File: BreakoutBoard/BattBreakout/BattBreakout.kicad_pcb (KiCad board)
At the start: 2 copper layers, 67.3 x 52.1 mm, 24 parts, among them Q4 IPB180N10S4-02, Q9 IPB180N10S4-02, U2 LM5050MK-1_NOPB, U3 LM5050MK-1_NOPB

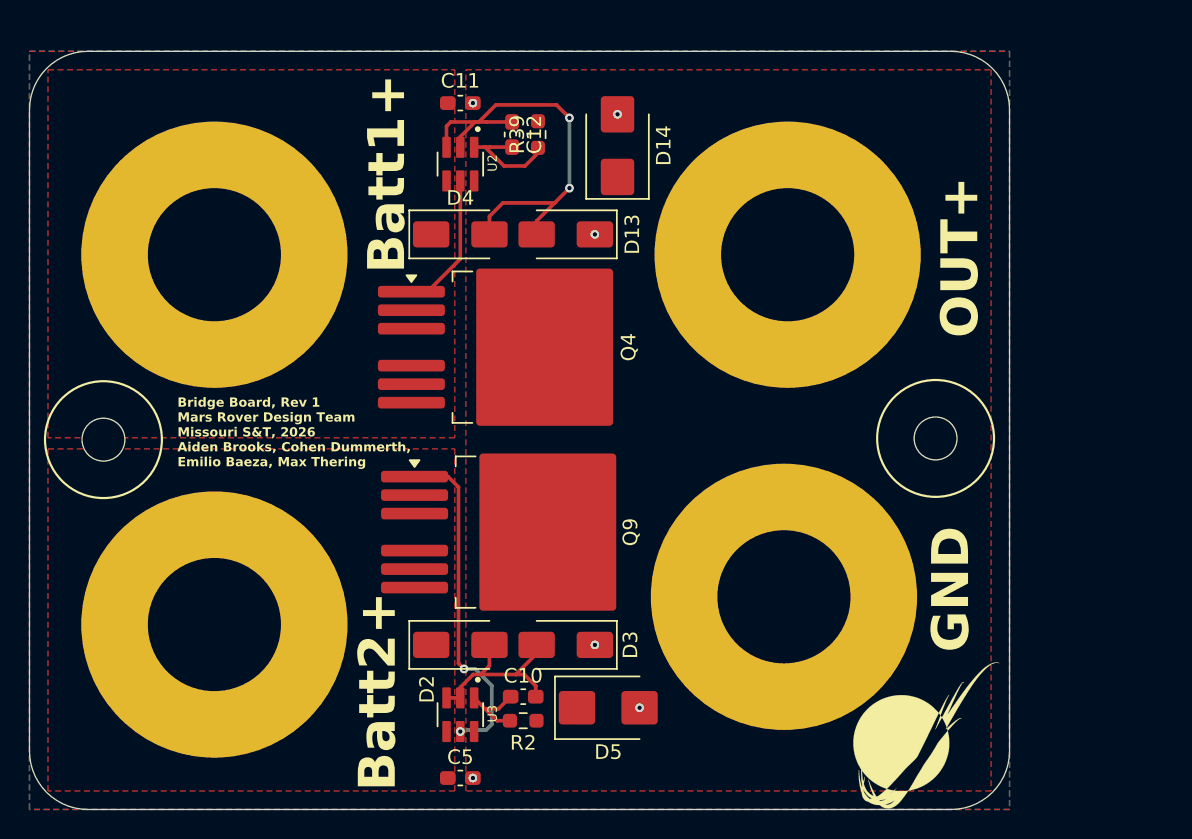
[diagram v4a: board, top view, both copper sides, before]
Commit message: Updated mosfet in schematic
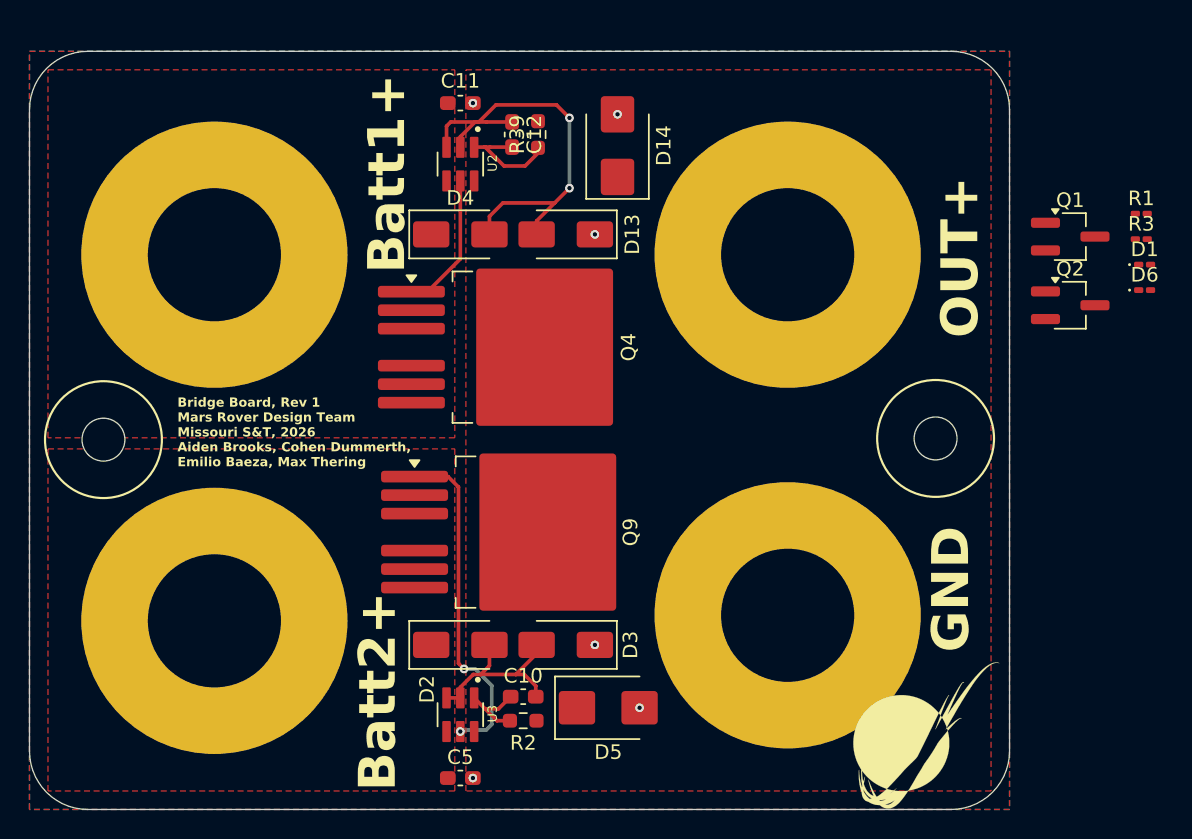
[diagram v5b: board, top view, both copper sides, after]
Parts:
- added D1: GRN, LED_SMD:LED_0201_0603Metric_Pad0.64x0.40mm_HandSolder, F.Cu at (107.1, 52.8)
- added D6: GRN, LED_SMD:LED_0201_0603Metric_Pad0.64x0.40mm_HandSolder, F.Cu at (107.1, 54.5)
- added Q1: BSS138, Package_TO_SOT_SMD:SOT-23W_Handsoldering, F.Cu at (102.0, 50.8)
- added Q2: BSS138, Package_TO_SOT_SMD:SOT-23W_Handsoldering, F.Cu at (102.0, 55.5)
- added R1: 6.8k, Resistor_SMD:R_0201_0603Metric_Pad0.64x0.40mm_HandSolder, F.Cu at (106.8, 49.2)
- added R3: 6.8k, Resistor_SMD:R_0201_0603Metric_Pad0.64x0.40mm_HandSolder, F.Cu at (106.8, 51.0)
- moved V3 39.4 mm to (82.5, 76.8)
- moved V2 39.2 mm to (43.2, 77.2)

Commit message: Added LEDS to layout
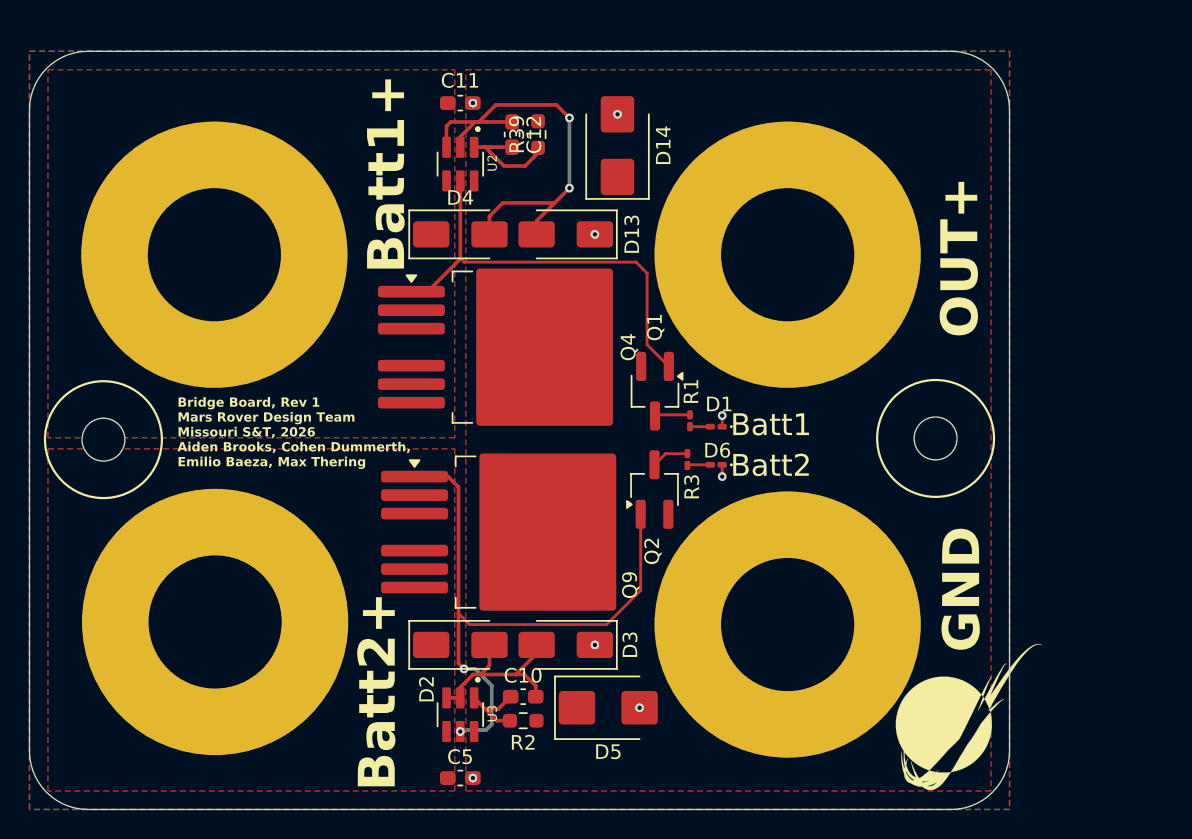
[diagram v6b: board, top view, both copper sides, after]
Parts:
- moved V2 39.4 mm to (82.5, 77.5)
- moved V3 39.3 mm to (43.2, 77.3)
- moved R3 34.7 mm to (75.7, 66.1), turned to 90 degrees
- moved R1 34.1 mm to (75.8, 63.5), turned to 90 degrees
- moved D6 31.8 mm to (77.6, 66.5), turned to 180 degrees
- moved D1 31.5 mm to (77.6, 63.9), turned to 180 degrees
- moved Q2 31.2 mm to (73.4, 68.2), turned to 90 degrees
- moved Q1 30.4 mm to (73.4, 61.4), turned to -90 degrees
- moved G1 3.19 mm to (95.0, 83.8)
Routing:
- net Net-(Q1-G): track 9.65 -> 29.9 mm
- net Net-(Q2-G): track 23.4 -> 42.4 mm
- net Net-(Q2-D): track 0.00 -> 2.58 mm
- net Net-(Q1-D): track 0.00 -> 2.44 mm
- net Net-(D6-A): track 0.00 -> 1.59 mm
- net GND: track 0.00 -> 1.58 mm, vias 6 -> 8
- net Net-(D1-A): track 0.00 -> 1.40 mm
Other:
- board text added: "Batt1"
- board text added: "Batt2"

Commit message: Fixed resistor footprints
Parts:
- R2, R39: footprint Resistor_SMD:R_0603_1608Metric_Pad0.98x0.95mm_HandSolder -> Resistor_SMD:R_0201_0603Metric_Pad0.64x0.40mm_HandSolder
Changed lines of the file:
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@@
 		)
 	)
-	(footprint "Resistor_SMD:R_0603_1608Metric_Pad0.98x0.95mm_HandSolder"
+	(footprint "Resistor_SMD:R_0201_0603Metric_Pad0.64x0.40mm_HandSolder"
 		(layer "F.Cu")
 		(at 65.405 43.815 90)
-		(descr "Resistor SMD 0603 (1608 Metric), square (rectangular) end terminal, IPC-7351 nominal with elongated pad for handsoldering. (Body size source: IPC-SM-782 page 72, https://www.pcb-3d.com/wordpress/wp-content/uploads/ipc-sm-782a_amendment_1_and_2.pdf), generated with kicad-footprint-generator")
+		(descr "Resistor SMD 0201 (0603 Metric), square (rectangular) end terminal, IPC-7351 nominal with elongated pad for handsoldering. (Body size source: https://www.vishay.com/docs/20052/crcw0201e3.pdf), generated with kicad-footprint-generator")
 		(tags "resistor handsolder")
 		(property "Reference" "R39"
-			(at 0 -1.43 90)
+			(at 0 -1.05 90)
 			(layer "F.SilkS")
 			(effects
@@
 		)
 		(property "Value" "100"
-			(at 0 1.43 90)
+			(at 0 1.05 90)
 			(layer "F.Fab")
 			(effects
@@
 		(attr smd)
 		(fp_line
-			(start -0.254724 -0.5225)
-			(end 0.254724 -0.5225)
-			(stroke
-				(width 0.12)
-				(type solid)
-			)
-			(layer "F.SilkS")
-		)
-		(fp_line
-			(start -0.254724 0.5225)
-			(end 0.254724 0.5225)
-			(stroke
-				(width 0.12)
-				(type solid)
-			)
-			(layer "F.SilkS")
-		)
-		(fp_line
-			(start 1.65 -0.73)
-			(end 1.65 0.73)
+			(start 0.88 -0.35)
+			(end 0.88 0.35)
 			(stroke
 				(width 0.05)
@@
 		)
 		(fp_line
-			(start -1.65 -0.73)
-			(end 1.65 -0.73)
+			(start -0.88 -0.35)
+			(end 0.88 -0.35)
 			(stroke
 				(width 0.05)
@@
 		)
 		(fp_line
-			(start 1.65 0.73)
-			(end -1.65 0.73)
+			(start 0.88 0.35)
+			(end -0.88 0.35)
 			(stroke
 				(width 0.05)
@@
 		)
 		(fp_line
-			(start -1.65 0.73)
-			(end -1.65 -0.73)
+			(start -0.88 0.35)
+			(end -0.88 -0.35)
 			(stroke
 				(width 0.05)
@@
 		)
 		(fp_line
-			(start 0.8 -0.4125)
-			(end 0.8 0.4125)
+			(start 0.3 -0.15)
+			(end 0.3 0.15)
 			(stroke
 				(width 0.1)
@@
 		)
 		(fp_line
-			(start -0.8 -0.4125)
-			(end 0.8 -0.4125)
+			(start -0.3 -0.15)
+			(end 0.3 -0.15)
 			(stroke
 				(width 0.1)
@@
 		)
 		(fp_line
-			(start 0.8 0.4125)
-			(end -0.8 0.4125)
+			(start 0.3 0.15)
+			(end -0.3 0.15)
 			(stroke
 				(width 0.1)
@@
 		)
 		(fp_line
-			(start -0.8 0.4125)
-			(end -0.8 -0.4125)
+			(start -0.3 0.15)
+			(end -0.3 -0.15)
 			(stroke
 				(width 0.1)
@@
 		)
 		(fp_text user "${REFERENCE}"
-			(at 0 0 90)
+			(at 0 -0.68 90)
 			(layer "F.Fab")
 			(effects
 				(font
-					(size 0.4 0.4)
-					(thickness 0.06)
+					(size 0.25 0.25)
+					(thickness 0.04)
 				)
 			)
 		)
+		(pad "" smd roundrect
+			(at -0.4325 0 90)
+			(size 0.458 0.36)
+			(layers "F.Paste")
+			(roundrect_rratio 0.25)
+		)
+		(pad "" smd roundrect
+			(at 0.4325 0 90)
+			(size 0.458 0.36)
+			(layers "F.Paste")
+			(roundrect_rratio 0.25)
+		)
 		(pad "1" smd roundrect
-			(at -0.9125 0 90)
-			(size 0.975 0.95)
-			(layers "F.Cu" "F.Mask" "F.Paste")
+			(at -0.4075 0 90)
+			(size 0.635 0.4)
+			(layers "F.Cu" "F.Mask")
 			(roundrect_rratio 0.25)
 			(net 8 "Net-(U2-VS)")
@@
 		)
 		(pad "2" smd roundrect
-			(at 0.9125 0 90)
-			(size 0.975 0.95)
-			(layers "F.Cu" "F.Mask" "F.Paste")
+			(at 0.4075 0 90)
+			(size 0.635 0.4)
+			(layers "F.Cu" "F.Mask")
 			(roundrect_rratio 0.25)
 			(net 2 "+24V")
@@
 		)
 		(embedded_fonts no)
-		(model "${KICAD9_3DMODEL_DIR}/Resistor_SMD.3dshapes/R_0603_1608Metric.step"
+		(model "${KICAD9_3DMODEL_DIR}/Resistor_SMD.3dshapes/R_0201_0603Metric.step"
 			(offset
 				(xyz 0 0 0)
@@
 		)
 	)
-	(footprint "Resistor_SMD:R_0603_1608Metric_Pad0.98x0.95mm_HandSolder"
+	(footprint "Resistor_SMD:R_0201_0603Metric_Pad0.64x0.40mm_HandSolder"
 		(layer "F.Cu")
 		(at 64.389 84.074)
-		(descr "Resistor SMD 0603 (1608 Metric), square (rectangular) end terminal, IPC-7351 nominal with elongated pad for handsoldering. (Body size source: IPC-SM-782 page 72, https://www.pcb-3d.com/wordpress/wp-content/uploads/ipc-sm-782a_amendment_1_and_2.pdf), generated with kicad-footprint-generator")
+		(descr "Resistor SMD 0201 (0603 Metric), square (rectangular) end terminal, IPC-7351 nominal with elongated pad for handsoldering. (Body size source: https://www.vishay.com/docs/20052/crcw0201e3.pdf), generated with kicad-footprint-generator")
 		(tags "resistor handsolder")
 		(property "Reference" "R2"
-			(at 0 1.524 0)
+			(at 0 -1.05 0)
 			(layer "F.SilkS")
 			(effects
@@
 		)
 		(property "Value" "100"
-			(at 0 1.43 0)
+			(at 0 1.05 0)
 			(layer "F.Fab")
 			(effects
@@
 		(attr smd)
 		(fp_line
-			(start -0.254724 -0.5225)
-			(end 0.254724 -0.5225)
-			(stroke
-				(width 0.12)
-				(type solid)
-			)
-			(layer "F.SilkS")
-		)
-		(fp_line
-			(start -0.254724 0.5225)
-			(end 0.254724 0.5225)
-			(stroke
-				(width 0.12)
-				(type solid)
-			)
-			(layer "F.SilkS")
-		)
-		(fp_line
-			(start -1.65 -0.73)
-			(end 1.65 -0.73)
+			(start -0.88 -0.35)
+			(end 0.88 -0.35)
 			(stroke
 				(width 0.05)
@@
 		)
 		(fp_line
-			(start -1.65 0.73)
-			(end -1.65 -0.73)
+			(start -0.88 0.35)
+			(end -0.88 -0.35)
 			(stroke
 				(width 0.05)
@@
 		)
 		(fp_line
-			(start 1.65 -0.73)
-			(end 1.65 0.73)
+			(start 0.88 -0.35)
+			(end 0.88 0.35)
 			(stroke
 				(width 0.05)
@@
 		)
 		(fp_line
-			(start 1.65 0.73)
-			(end -1.65 0.73)
+			(start 0.88 0.35)
+			(end -0.88 0.35)
 			(stroke
 				(width 0.05)
@@
 		)
 		(fp_line
-			(start -0.8 -0.4125)
-			(end 0.8 -0.4125)
+			(start -0.3 -0.15)
+			(end 0.3 -0.15)
 			(stroke
 				(width 0.1)
@@
 		)
 		(fp_line
-			(start -0.8 0.4125)
-			(end -0.8 -0.4125)
+			(start -0.3 0.15)
+			(end -0.3 -0.15)
 			(stroke
 				(width 0.1)
@@
 		)
 		(fp_line
-			(start 0.8 -0.4125)
-			(end 0.8 0.4125)
+			(start 0.3 -0.15)
+			(end 0.3 0.15)
 			(stroke
 				(width 0.1)
@@
 		)
 		(fp_line
-			(start 0.8 0.4125)
-			(end -0.8 0.4125)
+			(start 0.3 0.15)
+			(end -0.3 0.15)
 			(stroke
 				(width 0.1)
@@
 		)
 		(fp_text user "${REFERENCE}"
-			(at 0 0 0)
+			(at 0 -0.68 0)
 			(layer "F.Fab")
 			(effects
 				(font
-					(size 0.4 0.4)
-					(thickness 0.06)
+					(size 0.25 0.25)
+					(thickness 0.04)
 				)
 			)
 		)
+		(pad "" smd roundrect
+			(at -0.4325 0)
+			(size 0.458 0.36)
+			(layers "F.Paste")
+			(roundrect_rratio 0.25)
+		)
+		(pad "" smd roundrect
+			(at 0.4325 0)
+			(size 0.458 0.36)
+			(layers "F.Paste")
+			(roundrect_rratio 0.25)
+		)
 		(pad "1" smd roundrect
-			(at -0.9125 0)
-			(size 0.975 0.95)
-			(layers "F.Cu" "F.Mask" "F.Paste")
+			(at -0.4075 0)
+			(size 0.635 0.4)
+			(layers "F.Cu" "F.Mask")
 			(roundrect_rratio 0.25)
 			(net 5 "Net-(U3-VS)")
@@
 		)
 		(pad "2" smd roundrect
-			(at 0.9125 0)
-			(size 0.975 0.95)
-			(layers "F.Cu" "F.Mask" "F.Paste")
+			(at 0.4075 0)
+			(size 0.635 0.4)
+			(layers "F.Cu" "F.Mask")
 			(roundrect_rratio 0.25)
 			(net 2 "+24V")
@@
 		)
 		(embedded_fonts no)
-		(model "${KICAD9_3DMODEL_DIR}/Resistor_SMD.3dshapes/R_0603_1608Metric.step"
+		(model "${KICAD9_3DMODEL_DIR}/Resistor_SMD.3dshapes/R_0201_0603Metric.step"
 			(offset
 				(xyz 0 0 0)
